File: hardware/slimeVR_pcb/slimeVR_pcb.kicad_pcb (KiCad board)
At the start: 2 copper layers, 39 x 41 mm, 46 parts, among them J1 USB_C_Receptacle_USB2.0_16P, Q1 Q_Dual_NMOS_S1G1S2G2D2D2D1D1, SW1 SW_SPDT, SW3 SW_Push, U1 ESP32-S2-WROVER, U10 AP2112K-3.3, U2 TP4057, U3 ICM-45686, U5 QMC6309, U6 TPS25200DRVR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

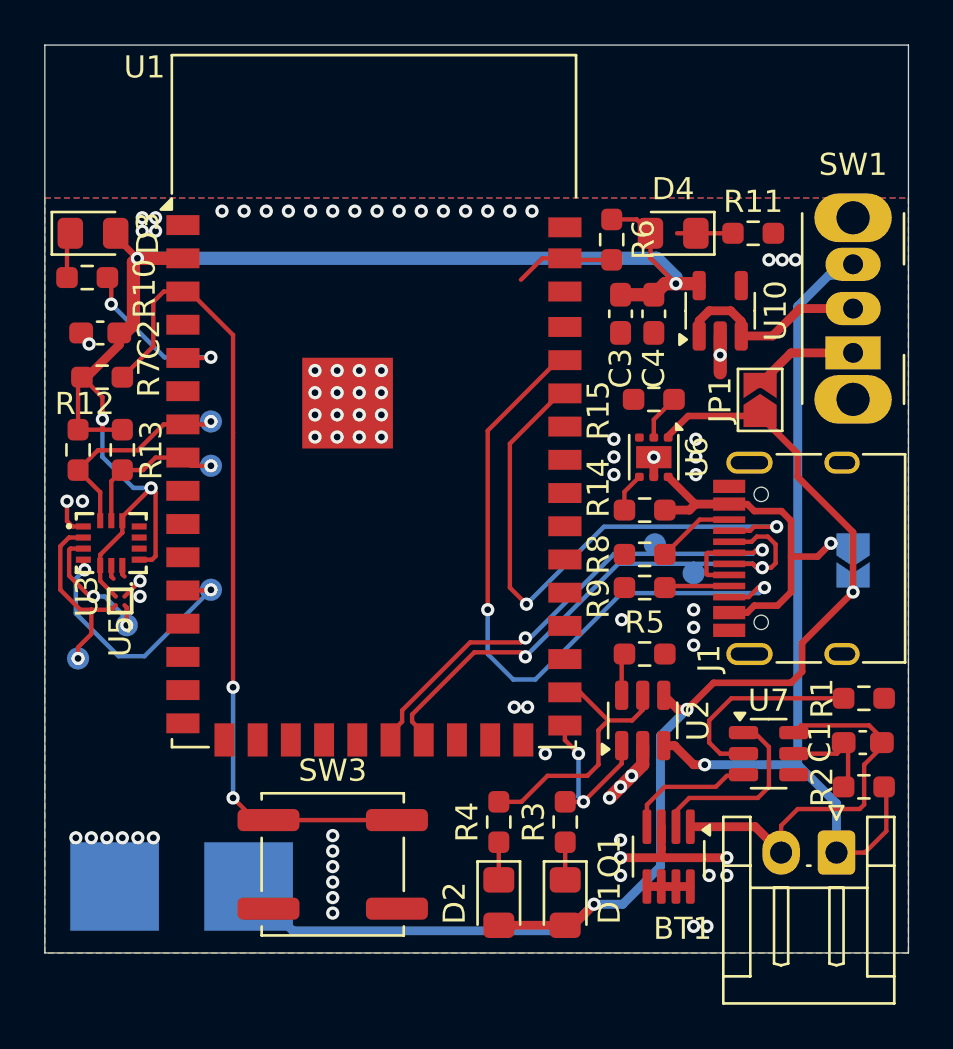
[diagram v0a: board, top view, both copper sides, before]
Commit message: implement garfields suggestions, cleanup board, add TPs
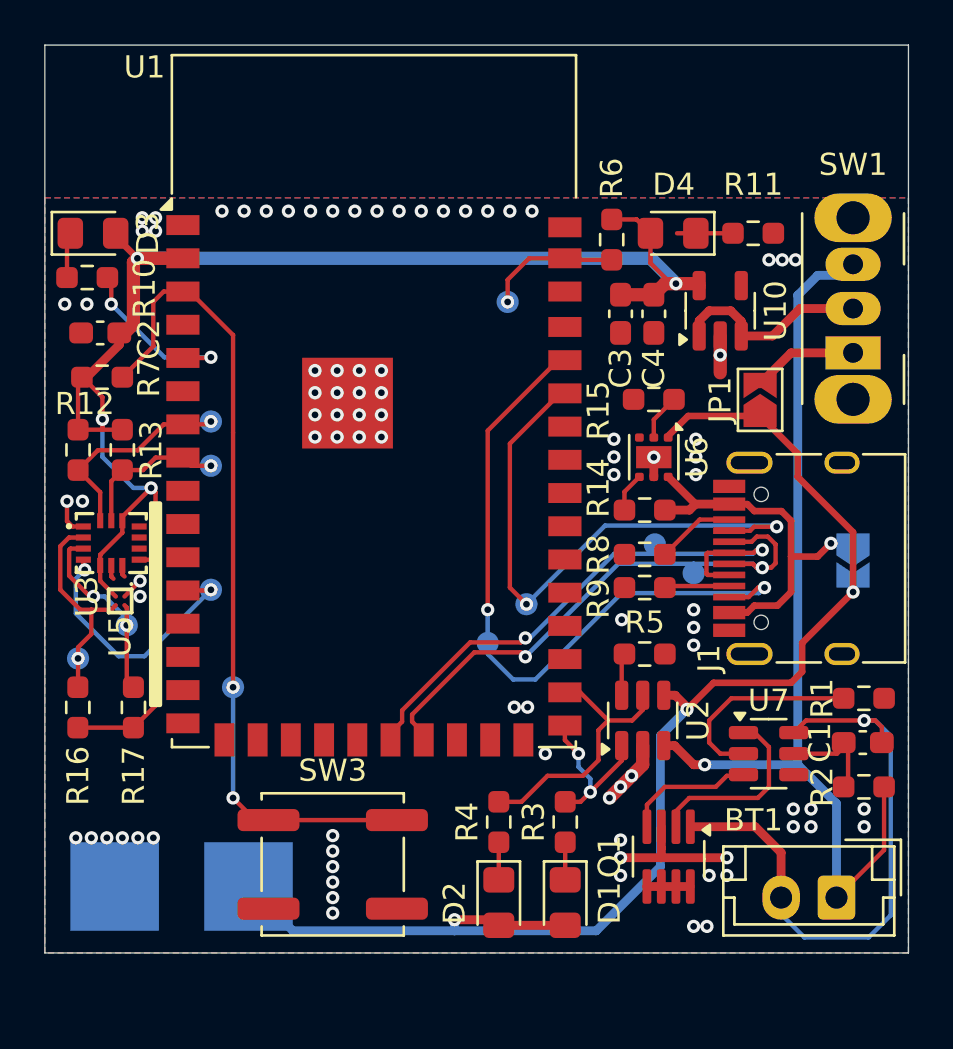
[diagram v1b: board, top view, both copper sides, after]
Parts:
- added R16: 1k, Resistor_SMD:R_0603_1608Metric_Pad0.98x0.95mm_HandSolder, F.Cu at (145.5, 66.4)
- added R17: 1k, Resistor_SMD:R_0603_1608Metric_Pad0.98x0.95mm_HandSolder, F.Cu at (148.0, 66.4)
- added TP10: EN, TestPoint:TestPoint_Pad_D1.0mm, B.Cu at (164.9, 48.1)
- added TP11: BOOT, TestPoint:TestPoint_Pad_D1.0mm, B.Cu at (152.5, 65.5)
- added TP12: TX, TestPoint:TestPoint_Pad_D1.0mm, B.Cu at (165.7, 61.8)
- added TP13: RX, TestPoint:TestPoint_Pad_D1.0mm, B.Cu at (164.0, 63.5)
- BT1: footprint Connector_JST:JST_EH_S2B-EH_1x02_P2.50mm_Horizontal -> Connector_JST:JST_EH_B2B-EH-A_1x02_P2.50mm_Vertical
- moved BT1 2.03 mm to (179.8, 75.0)
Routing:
- net +3V3: track 65.9 -> 76.5 mm
- net -BATT: track 17.8 -> 27.8 mm, vias 0 -> 1
- net +BATT: track 39.5 -> 43.1 mm
- net /SCL_IMU: track 6.48 -> 9.40 mm
- net /EN: track 4.53 -> 6.13 mm, vias 0 -> 1
- net +5V: track 59.4 -> 60.7 mm
- net /SDA_IMU: track 8.58 -> 9.88 mm
- net GND: vias 81 -> 88
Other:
- board text added: "+ -"

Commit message: add decoupleing caps
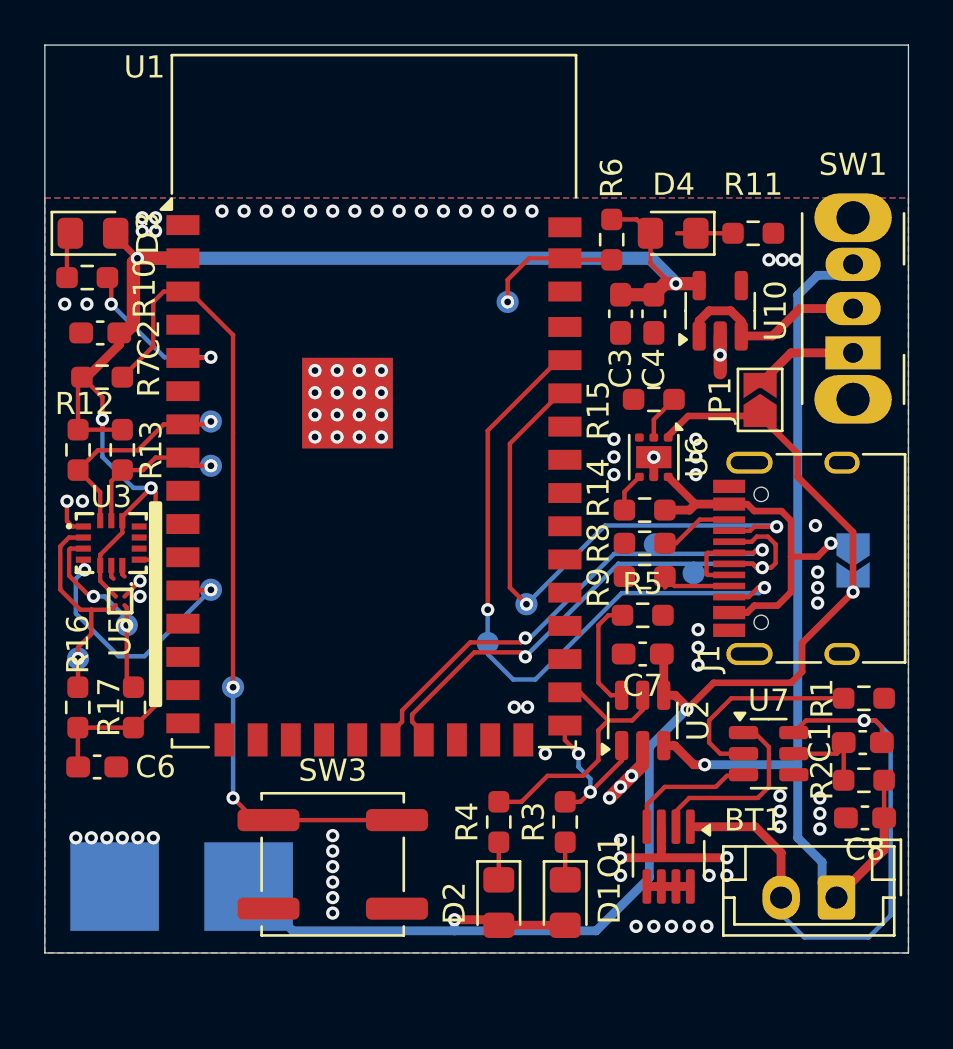
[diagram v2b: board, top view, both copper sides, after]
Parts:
- added C6: 1u, Capacitor_SMD:C_0603_1608Metric_Pad1.08x0.95mm_HandSolder, F.Cu at (146.4, 69.1)
- added C7: 100n, Capacitor_SMD:C_0603_1608Metric_Pad1.08x0.95mm_HandSolder, F.Cu at (171.0, 64.0)
- added C8: 100n, Capacitor_SMD:C_0603_1608Metric_Pad1.08x0.95mm_HandSolder, F.Cu at (181.0, 71.4)
- C4: value 1u -> 10u
- R12, R13, R16, R17: value 1k -> 4k7
- moved R5 1.75 mm to (171.0, 62.2)
- moved R8 0.50 mm to (171.1, 59.0)
- moved R9 0.50 mm to (171.1, 60.5)
- moved R2 0.30 mm to (181.0, 69.7)
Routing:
- net Net-(U2-PROG): track 1.91 -> 5.16 mm
- net +5V: track 60.7 -> 62.6 mm
- net +3V3: track 76.5 -> 78.3 mm
- net GND: track 15.6 -> 15.8 mm, vias 88 -> 94
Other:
- board text added: "+"
- board text added: "-"
- board text removed: "+ -"

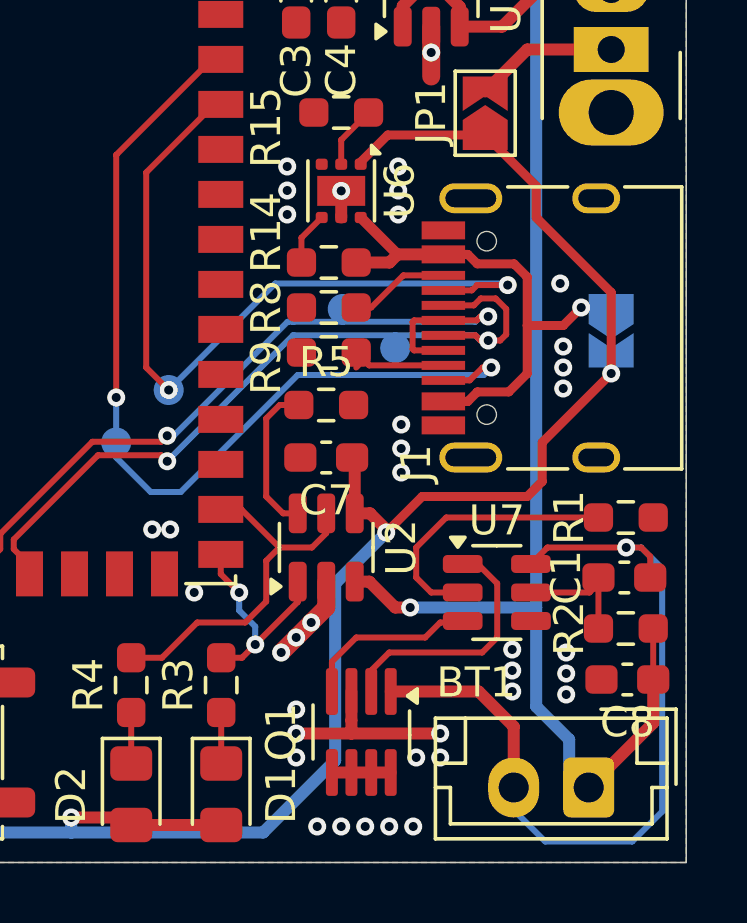
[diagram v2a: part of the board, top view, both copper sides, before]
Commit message: cleanup silkscreen, ground unused open-drain
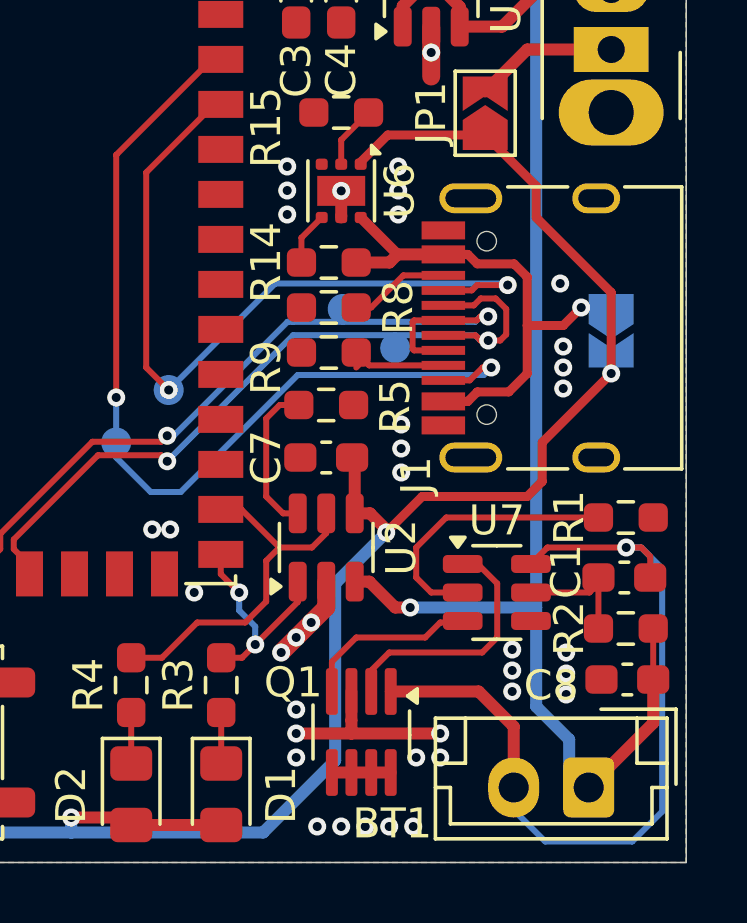
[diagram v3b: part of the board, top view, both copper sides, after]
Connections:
- U6 pad 3: unconnected-(U6-~{FAULT}-Pad3) -> GND

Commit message: add solderjumpers for charging signals
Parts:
- added JP3: SolderJumper_2_Open, Jumper:SolderJumper-2_P1.3mm_Open_TrianglePad1.0x1.5mm, F.Cu at (161.0, 71.5)
- added JP4: SolderJumper_2_Open, Jumper:SolderJumper-2_P1.3mm_Open_TrianglePad1.0x1.5mm, F.Cu at (161.0, 74.0)
- moved SW3 2.90 mm to (154.1, 73.5)
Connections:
- U1 pad 20: unconnected-(U1-IO17-Pad20) -> Net-(JP4-B)
- U1 pad 21: unconnected-(U1-IO18-Pad21) -> Net-(JP3-B)
- U1 pad 27: /BAT_CHG -> unconnected-(U1-IO33-Pad27)
- U1 pad 28: /BAT_FULL -> unconnected-(U1-IO34-Pad28)
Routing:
- net Net-(JP4-B): track 0.00 -> 7.64 mm
- net Net-(JP3-B): track 0.00 -> 4.52 mm
- net /BAT_CHG: track 7.48 -> 11.3 mm, vias 2 -> 0
- net /BAT_FULL: track 12.2 -> 12.8 mm
- net GND: vias 94 -> 96

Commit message: cleanup pcb
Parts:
- moved TP6 0.94 mm to (146.3, 64.7)
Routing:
- net /SDA_IMU: track 9.88 -> 11.0 mm
- net /SCL_IMU: track 9.40 -> 9.95 mm
- net GND: vias 96 -> 97

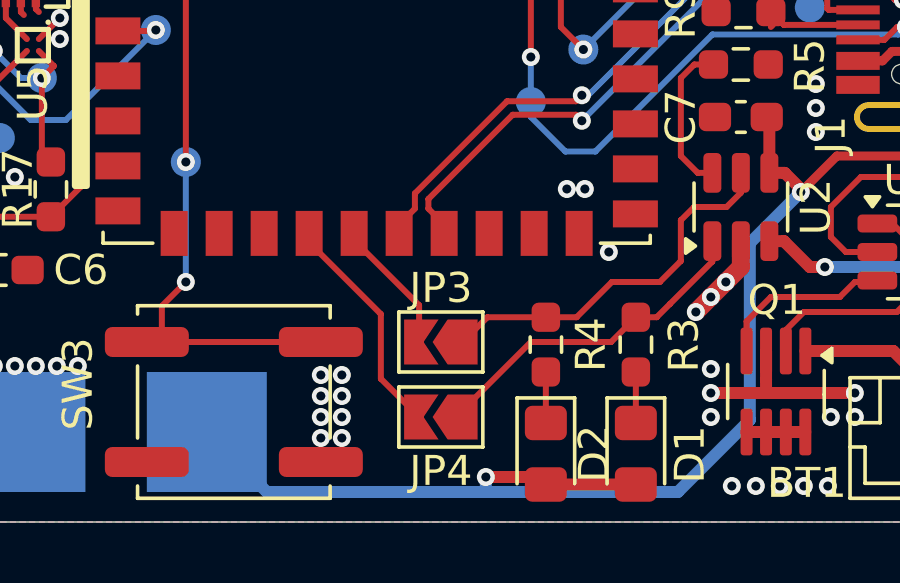
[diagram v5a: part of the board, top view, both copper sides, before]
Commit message: replace charging signal jumpers with resistors these allow the internal ESD diodes of the ESP32S2 to clamp the valotage to safe levels
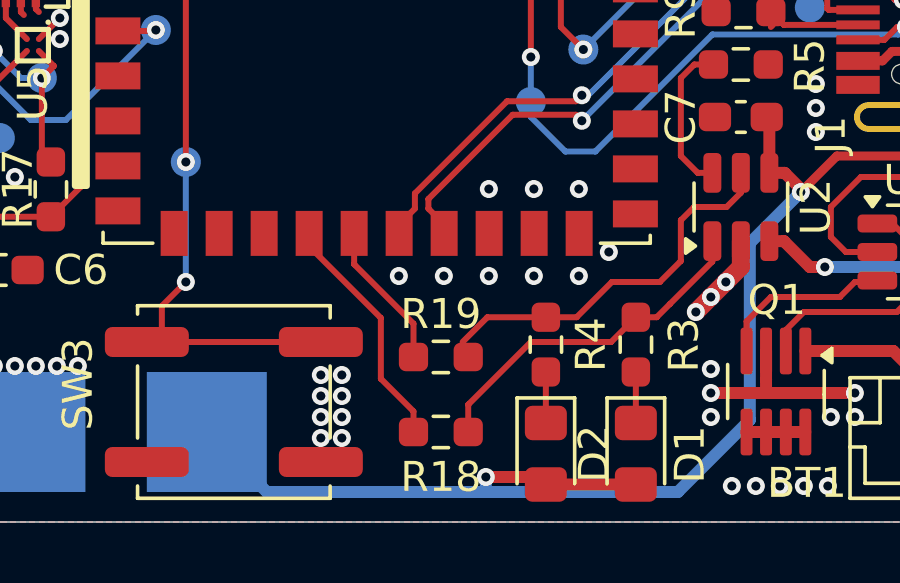
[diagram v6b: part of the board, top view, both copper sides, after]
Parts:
- removed JP3, JP4: SolderJumper_2_Open, Jumper:SolderJumper-2_P1.3mm_Open_TrianglePad1.0x1.5mm
- added R18: 330k, Resistor_SMD:R_0603_1608Metric_Pad0.98x0.95mm_HandSolder, F.Cu at (161.0, 74.5)
- added R19: 330k, Resistor_SMD:R_0603_1608Metric_Pad0.98x0.95mm_HandSolder, F.Cu at (161.0, 72.0)
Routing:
- net GND: vias 97 -> 103

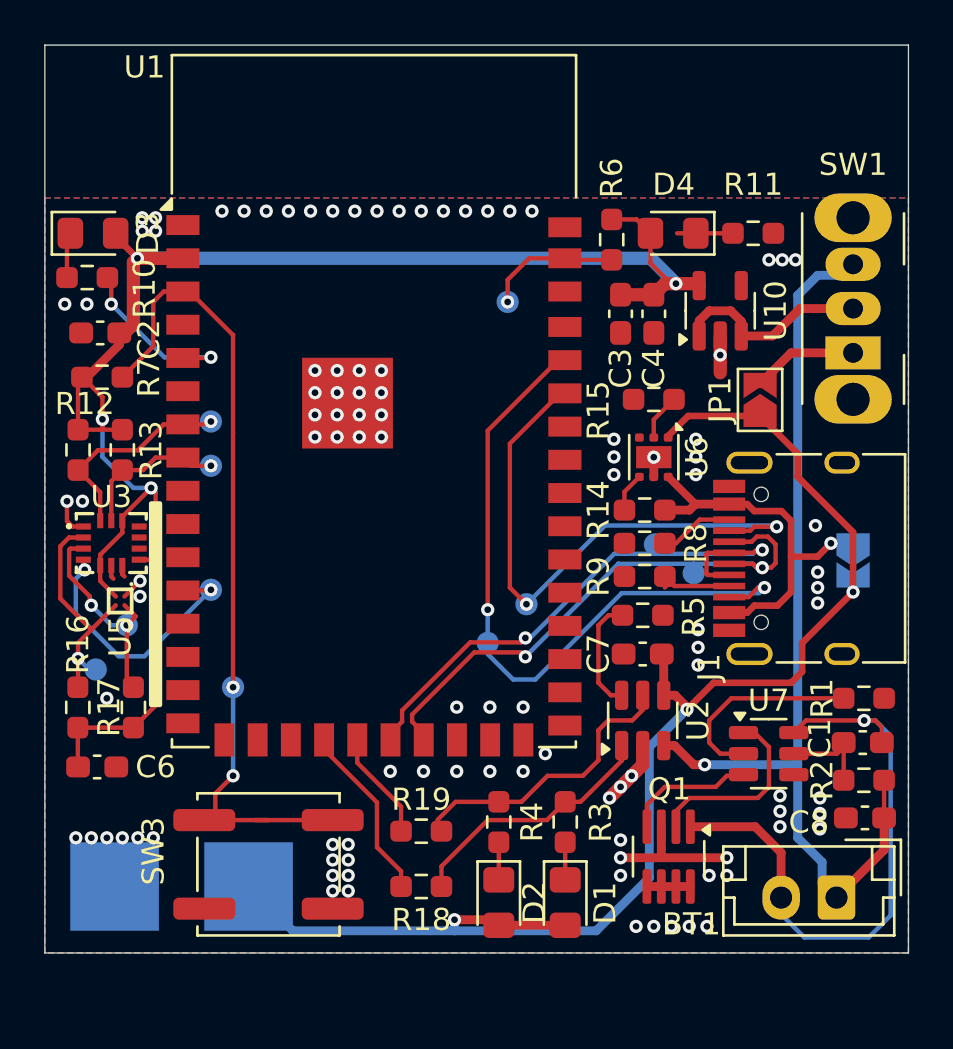
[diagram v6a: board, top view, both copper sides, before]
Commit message: add mounting holes
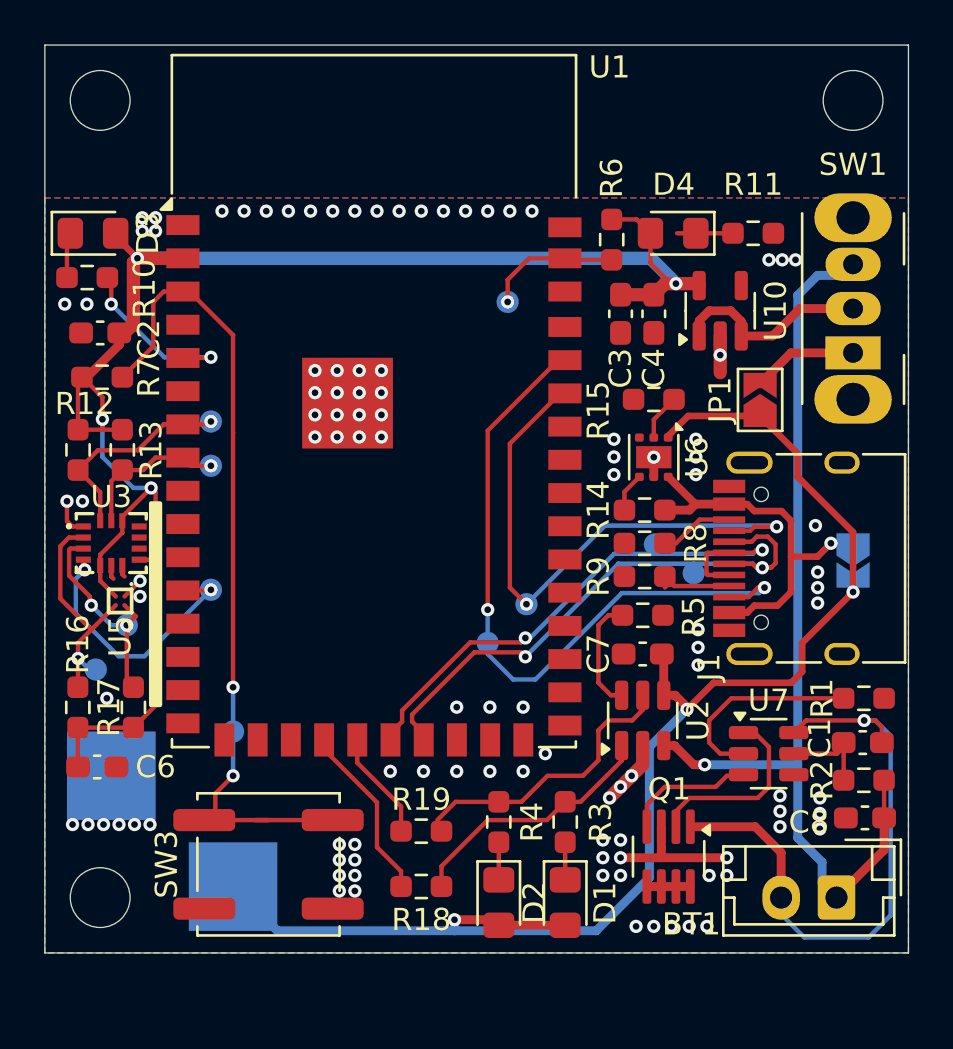
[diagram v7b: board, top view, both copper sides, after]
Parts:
- added REF**: MountingHole_2.7mm_M2.5_ISO14580, MountingHole:MountingHole_2.7mm_M2.5_ISO14580, F.Cu at (146.5, 39.0)
- added REF**: MountingHole_2.7mm_M2.5_ISO14580, MountingHole:MountingHole_2.7mm_M2.5_ISO14580, F.Cu at (180.5, 39.0)
- added REF**: MountingHole_2.7mm_M2.5_ISO14580, MountingHole:MountingHole_2.7mm_M2.5_ISO14580, F.Cu at (146.5, 75.0)
- moved TP1 5.00 mm to (147.0, 69.5)
- moved TP11 2.00 mm to (152.5, 67.5)
- moved TP2 0.70 mm to (152.5, 74.5)
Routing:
- net +5V: track 62.6 -> 63.3 mm
- net GND: vias 103 -> 106
